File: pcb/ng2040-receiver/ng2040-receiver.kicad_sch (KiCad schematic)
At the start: 15 parts, among them J1 DB15_F, U1 RP2040-Zero, U2 NRF24L01_Breakout

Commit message: Titling schematic
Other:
- company: (none) -> @partlyhuman
- title: (none) -> NG2040 Receiver
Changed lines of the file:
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@@
 	(generator_version "8.0")
 	(paper "A4")
+	(title_block
+		(title "NG2040 Receiver")
+		(rev "4")
+		(company "@partlyhuman")
+	)
 	(junction
 		(at 86.36 124.46)
@@
 		)
 		(instances
-			(project "NeoGeoDB15Wireless"
+			(project "ng2040-receiver"
 				(path "/e91880d7-e1f1-43ba-b9bf-5f0fc90655d2"
 					(reference "R4")
@@
 		)
 		(instances
-			(project "NeoGeoDB15Wireless"
+			(project "ng2040-receiver"
 				(path "/e91880d7-e1f1-43ba-b9bf-5f0fc90655d2"
 					(reference "U2")
@@
 		)
 		(instances
-			(project "NeoGeoDB15Wireless"
+			(project "ng2040-receiver"
 				(path "/e91880d7-e1f1-43ba-b9bf-5f0fc90655d2"
 					(reference "R3")
@@
 		)
 		(instances
-			(project "NeoGeoDB15Wireless"
+			(project "ng2040-receiver"
 				(path "/e91880d7-e1f1-43ba-b9bf-5f0fc90655d2"
 					(reference "R6")
@@
 		)
 		(instances
-			(project "NeoGeoDB15Wireless"
+			(project "ng2040-receiver"
 				(path "/e91880d7-e1f1-43ba-b9bf-5f0fc90655d2"
 					(reference "R10")
@@
 		)
 		(instances
-			(project "NeoGeoDB15Wireless"
+			(project "ng2040-receiver"
 				(path "/e91880d7-e1f1-43ba-b9bf-5f0fc90655d2"
 					(reference "C1")
@@
 		)
 		(instances
-			(project "NeoGeoDB15Wireless"
+			(project "ng2040-receiver"
 				(path "/e91880d7-e1f1-43ba-b9bf-5f0fc90655d2"
 					(reference "U1")
@@
 		)
 		(instances
-			(project "NeoGeoDB15Wireless"
+			(project "ng2040-receiver"
 				(path "/e91880d7-e1f1-43ba-b9bf-5f0fc90655d2"
 					(reference "#PWR01")
@@
 		)
 		(instances
-			(project "NeoGeoDB15Wireless"
+			(project "ng2040-receiver"
 				(path "/e91880d7-e1f1-43ba-b9bf-5f0fc90655d2"
 					(reference "R5")
@@
 		)
 		(instances
-			(project "NeoGeoDB15Wireless"
+			(project "ng2040-receiver"
 				(path "/e91880d7-e1f1-43ba-b9bf-5f0fc90655d2"
 					(reference "R8")
@@
 		)
 		(instances
-			(project "NeoGeoDB15Wireless"
+			(project "ng2040-receiver"
 				(path "/e91880d7-e1f1-43ba-b9bf-5f0fc90655d2"
 					(reference "R1")
@@
 		)
 		(instances
-			(project "NeoGeoDB15Wireless"
+			(project "ng2040-receiver"
 				(path "/e91880d7-e1f1-43ba-b9bf-5f0fc90655d2"
 					(reference "#FLG02")
@@
 		)
 		(instances
-			(project "NeoGeoDB15Wireless"
+			(project "ng2040-receiver"
 				(path "/e91880d7-e1f1-43ba-b9bf-5f0fc90655d2"
 					(reference "#FLG01")
@@
 		)
 		(instances
-			(project "NeoGeoDB15Wireless"
+			(project "ng2040-receiver"
 				(path "/e91880d7-e1f1-43ba-b9bf-5f0fc90655d2"
 					(reference "#PWR02")
@@
 		)
 		(instances
-			(project "NeoGeoDB15Wireless"
+			(project "ng2040-receiver"
 				(path "/e91880d7-e1f1-43ba-b9bf-5f0fc90655d2"
 					(reference "#PWR03")
@@
 		)
 		(instances
-			(project "NeoGeoDB15Wireless"
+			(project "ng2040-receiver"
 				(path "/e91880d7-e1f1-43ba-b9bf-5f0fc90655d2"
 					(reference "J1")
@@
 		)
 		(instances
-			(project "NeoGeoDB15Wireless"
+			(project "ng2040-receiver"
 				(path "/e91880d7-e1f1-43ba-b9bf-5f0fc90655d2"
 					(reference "R2")
@@
 		)
 		(instances
-			(project "NeoGeoDB15Wireless"
+			(project "ng2040-receiver"
 				(path "/e91880d7-e1f1-43ba-b9bf-5f0fc90655d2"
 					(reference "R7")
@@
 		)
 		(instances
-			(project "NeoGeoDB15Wireless"
+			(project "ng2040-receiver"
 				(path "/e91880d7-e1f1-43ba-b9bf-5f0fc90655d2"
 					(reference "R9")
@@
 		)
 		(instances
-			(project "NeoGeoDB15Wireless"
+			(project "ng2040-receiver"
 				(path "/e91880d7-e1f1-43ba-b9bf-5f0fc90655d2"
 					(reference "C2")

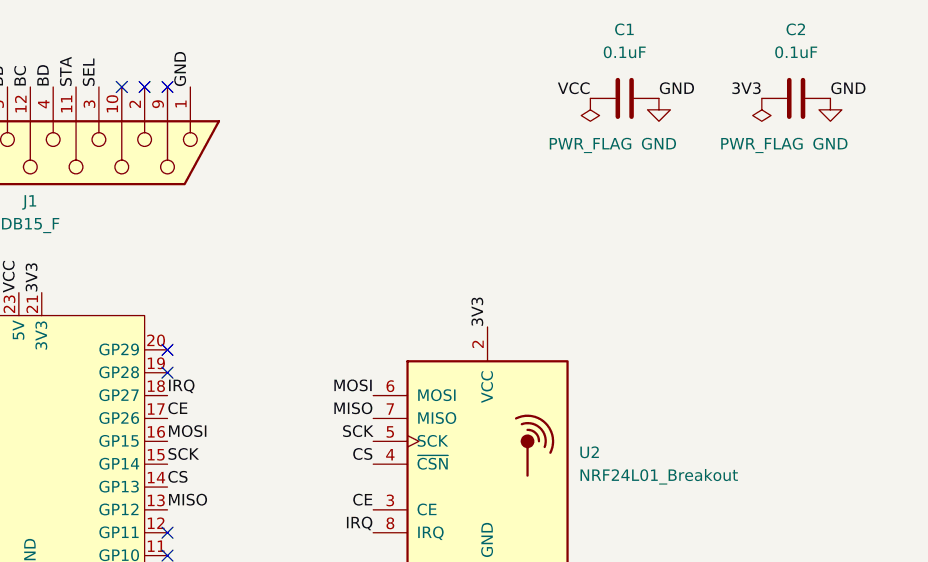
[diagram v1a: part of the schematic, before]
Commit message: Reworking controller board to put pico on back for LED to shine through
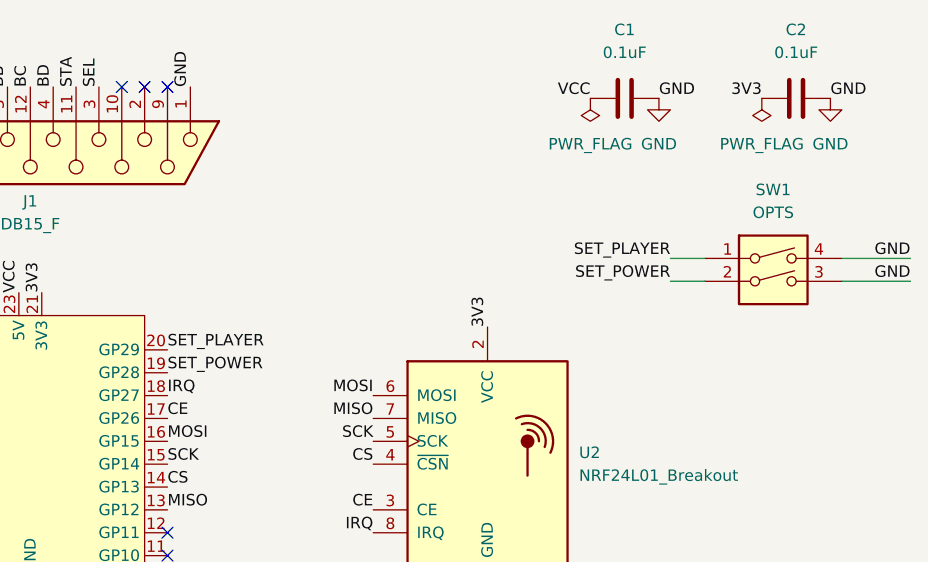
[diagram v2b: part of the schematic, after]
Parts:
- added SW1: OPTS, Button_Switch_SMD:SW_DIP_SPSTx02_Slide_6.7x6.64mm_W8.61mm_P2.54mm_LowProfile, symbol Switch:SW_DIP_x02
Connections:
- net GND: now also SW1.3, SW1.4
- net SET_POWER: now reaches U1.19 (GP28)
- net SET_POWER: now also SW1.2
- net SET_PLAYER: now reaches U1.20 (GP29)
- net SET_PLAYER: now also SW1.1
- no-connect marks 7 -> 5
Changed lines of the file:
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@@
-	)
-	(no_connect
-		(at 130.81 55.88)
-	)
-	(no_connect
-		(at 130.81 58.42)
 	)
 	(no_connect
@@
 	(wire
 		(pts
+			(xy 205.74 45.72) (xy 213.36 45.72)
+		)
+		(stroke
+			(width 0)
+			(type default)
+		)
+	)
+	(wire
+		(pts
 			(xy 64.77 130.81) (xy 91.44 130.81)
 		)
@@
 	(wire
 		(pts
+			(xy 186.69 48.26) (xy 190.5 48.26)
+		)
+		(stroke
+			(width 0)
+			(type default)
+		)
+	)
+	(wire
+		(pts
 			(xy 116.84 171.45) (xy 116.84 176.53)
 		)
@@
 	(wire
 		(pts
+			(xy 186.69 45.72) (xy 190.5 45.72)
+		)
+		(stroke
+			(width 0)
+			(type default)
+		)
+	)
+	(wire
+		(pts
 			(xy 64.77 162.56) (xy 116.84 162.56)
+		)
+		(stroke
+			(width 0)
+			(type default)
+		)
+	)
+	(wire
+		(pts
+			(xy 205.74 48.26) (xy 213.36 48.26)
 		)
 		(stroke
@@
 	)
 	(label "GND"
+		(at 213.36 45.72 180)
+		(fields_autoplaced yes)
+		(effects
+			(font
+				(size 1.27 1.27)
+			)
+			(justify right bottom)
+		)
+	)
+	(label "GND"
 		(at 115.57 83.82 270)
 		(fields_autoplaced yes)
@@
 		)
 	)
+	(label "GND"
+		(at 213.36 48.26 180)
+		(fields_autoplaced yes)
+		(effects
+			(font
+				(size 1.27 1.27)
+			)
+			(justify right bottom)
+		)
+	)
 	(label "BB"
 		(at 101.6 68.58 180)
@@
 		)
 	)
+	(label "SET_PLAYER"
+		(at 186.69 45.72 180)
+		(fields_autoplaced yes)
+		(effects
+			(font
+				(size 1.27 1.27)
+			)
+			(justify right bottom)
+		)
+	)
 	(label "SCK"
 		(at 130.81 68.58 0)
@@
 		)
 	)
+	(label "SET_POWER"
+		(at 186.69 48.26 180)
+		(fields_autoplaced yes)
+		(effects
+			(font
+				(size 1.27 1.27)
+			)
+			(justify right bottom)
+		)
+	)
 	(label "SEL"
 		(at 64.77 162.56 180)
@@
 		)
 	)
+	(label "SET_POWER"
+		(at 130.81 58.42 0)
+		(fields_autoplaced yes)
+		(effects
+			(font
+				(size 1.27 1.27)
+			)
+			(justify left bottom)
+		)
+	)
 	(label "VCC"
 		(at 177.8 27.94 180)
@@
 			)
 			(justify right bottom)
+		)
+	)
+	(label "SET_PLAYER"
+		(at 130.81 55.88 0)
+		(fields_autoplaced yes)
+		(effects
+			(font
+				(size 1.27 1.27)
+			)
+			(justify left bottom)
 		)
 	)
@@
 					(unit 1)
 				)
+			)
+		)
+	)
+	(symbol
+		(lib_id "Switch:SW_DIP_x02")
+		(at 198.12 48.26 0)
+		(unit 1)
+		(exclude_from_sim no)
+		(in_bom yes)
+		(on_board yes)
+		(dnp no)
+		(fields_autoplaced yes)
+		(property "Reference" "SW1"
+			(at 198.12 38.1 0)
+			(effects
+				(font
+					(size 1.27 1.27)
+				)
+			)
+		)
+		(property "Value" "OPTS"
+			(at 198.12 40.64 0)
+			(effects
+				(font
+					(size 1.27 1.27)
+				)
+			)
+		)
+		(property "Footprint" "Button_Switch_SMD:SW_DIP_SPSTx02_Slide_6.7x6.64mm_W8.61mm_P2.54mm_LowProfile"
+			(at 198.12 48.26 0)
+			(effects
+				(font
+					(size 1.27 1.27)
+				)
+				(hide yes)
+			)
+		)
+		(property "Datasheet" "~"
+			(at 198.12 48.26 0)
+			(effects
+				(font
+					(size 1.27 1.27)
+				)
+				(hide yes)
+			)
+		)
+		(property "Description" "2x DIP Switch, Single Pole Single Throw (SPST) switch, small symbol"
+			(at 198.12 48.26 0)
+			(effects
+				(font
+					(size 1.27 1.27)
+				)
+				(hide yes)
+			)
+		)
+		(property "Notes" ""
+			(at 198.12 48.26 0)
+			(effects
+				(font
+					(size 1.27 1.27)
+				)
+			)
+		)
+		(pin "4"
+		)
+		(pin "1"
+		)
+		(pin "2"
+		)
+		(pin "3"
+		)
+		(instances
+			(project "ng2040-receiver"
+				(path "/e91880d7-e1f1-43ba-b9bf-5f0fc90655d2"
+					(reference "SW1")
+					(unit 1)
+				)
